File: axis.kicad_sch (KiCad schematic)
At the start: 46 parts, among them J101 CORTEX-DEBUG, J102 JAE_DX07S016JA3, SW101 SW_Push, SW102 SW_Push, U101 TPS78433QWDRBRQ1, U102 ATSAMD51G, U103 BMM150, U104 BHI160, Y101 32k768

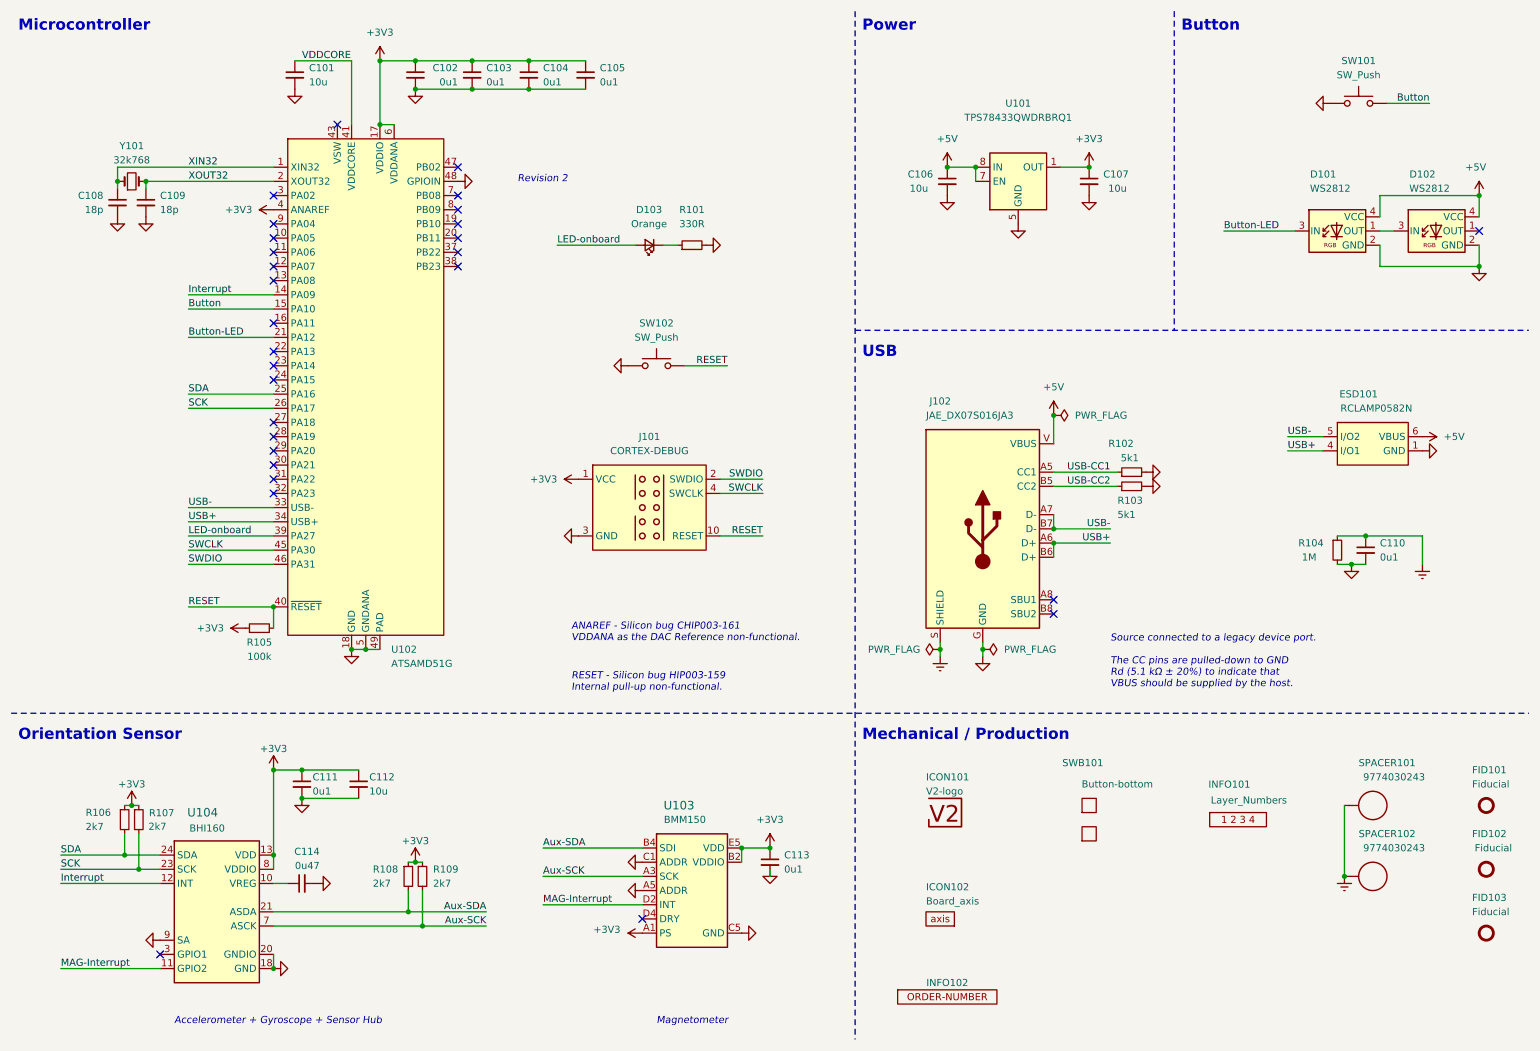
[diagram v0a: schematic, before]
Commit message: Replace standoffs
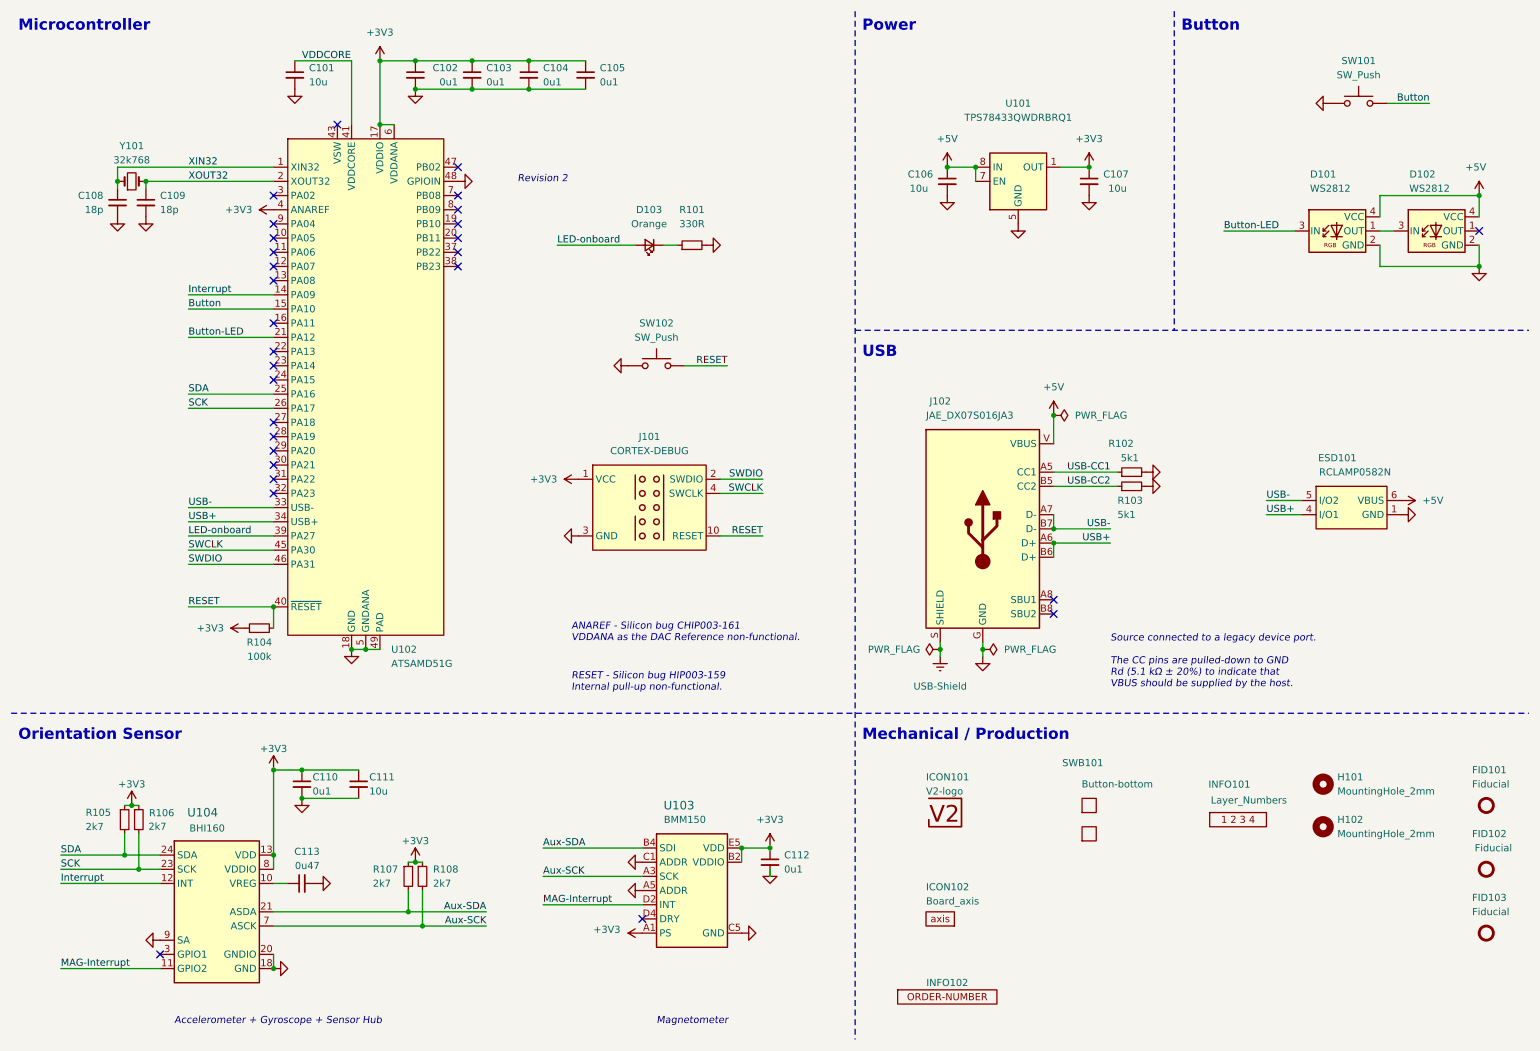
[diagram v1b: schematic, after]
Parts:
- removed C110: 0u1, Capacitor_SMD:C_0603_1608Metric, symbol Device:C_Small
- removed R104: 1M, Resistor_SMD:R_0603_1608Metric, symbol Device:R_Small
- removed SPACER101, SPACER102: 9774030243, V2_Spacer_Wurth:9774030243, symbol V2_Spacer_Wurth:9774030243
- added H101, H102: MountingHole_2mm, V2_Mechanical:MountingHole_2mm, symbol V2_Mechanical:MountingHole_2mm
- renumbered C111 to C110, C112 to C111, C113 to C112, C114 to C113, R105 to R104, R106 to R105, R107 to R106, R108 to R107, R109 to R108
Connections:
- net Earth renamed USB-Shield
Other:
- moved on the sheet: ESD101

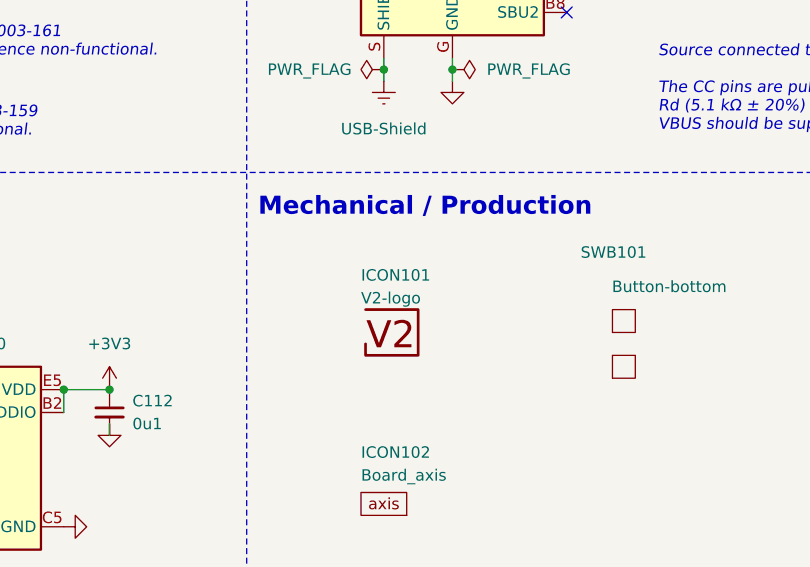
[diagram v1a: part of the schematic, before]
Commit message: Change capacitors
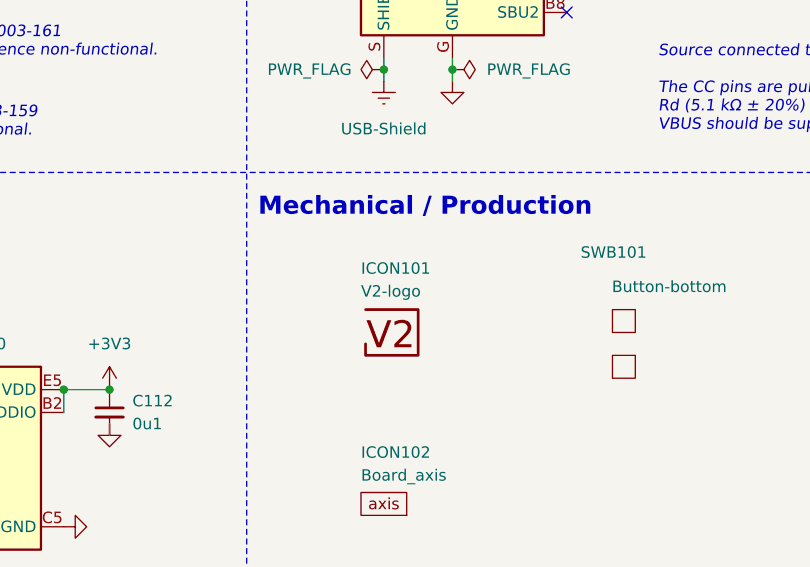
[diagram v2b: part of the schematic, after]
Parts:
- C106, C107: footprint Capacitor_SMD:C_0603_1608Metric -> Capacitor_SMD:C_0805_2012Metric
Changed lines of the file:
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@@
 	(title_block
 		(title "V2 axis")
-		(date "2025-10-26")
-		(rev "5")
+		(date "2025-11-16")
+		(rev "6")
 		(company "Versio Duo")
 		(comment 1 "Orientation Sensor")
@@
 			)
 		)
-		(property "Footprint" "Capacitor_SMD:C_0603_1608Metric"
+		(property "Footprint" "Capacitor_SMD:C_0805_2012Metric"
 			(at 205.74 43.18 0)
 			(effects
@@
 		(at 247.65 151.13 0)
 		(unit 1)
-		(exclude_from_sim no)
+		(exclude_from_sim yes)
 		(in_bom no)
 		(on_board yes)
@@
 			)
 		)
-		(property "Sim.Enable" "0"
-			(at 247.65 151.13 0)
-			(effects
-				(font
-					(size 1.27 1.27)
-				)
-				(hide yes)
-			)
-		)
 		(instances
 			(project ""
@@
 			)
 		)
-		(property "Footprint" "Capacitor_SMD:C_0603_1608Metric"
+		(property "Footprint" "Capacitor_SMD:C_0805_2012Metric"
 			(at 180.34 43.18 0)
 			(effects
@@
 		(dnp no)
 		(property "Reference" "ICON101"
-			(at 176.53 149.86 0)
+			(at 176.53 149.098 0)
 			(effects
 				(font
@@
 		)
 		(property "Value" "V2-logo"
-			(at 176.53 152.4 0)
+			(at 176.53 151.638 0)
 			(effects
 				(font

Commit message: Update
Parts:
- removed C110: 0u1, Capacitor_SMD:C_0603_1608Metric, symbol Device:C_Small
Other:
- moved on the sheet: C111
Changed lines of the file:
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@@
 	)
 	(junction
-		(at 64.77 148.59)
-		(diameter 0)
-		(color 0 0 0 0)
-	)
-	(junction
 		(at 105.41 26.67)
 		(diameter 0)
@@
 	)
 	(junction
-		(at 64.77 153.67)
-		(diameter 0)
-		(color 0 0 0 0)
-	)
-	(junction
 		(at 85.09 165.1)
 		(diameter 0)
@@
 	(wire
 		(pts
-			(xy 59.69 148.59) (xy 64.77 148.59)
-		)
-		(stroke
-			(width 0)
-			(type default)
-		)
-	)
-	(wire
-		(pts
 			(xy 148.59 167.64) (xy 148.59 166.37)
 		)
@@
 	(wire
 		(pts
-			(xy 64.77 153.67) (xy 74.93 153.67)
-		)
-		(stroke
-			(width 0)
-			(type default)
-		)
-	)
-	(wire
-		(pts
 			(xy 83.82 170.18) (xy 83.82 173.99)
 		)
@@
 	(wire
 		(pts
-			(xy 64.77 148.59) (xy 74.93 148.59)
+			(xy 59.69 148.59) (xy 64.77 148.59)
 		)
 		(stroke
@@
 	)
 	(symbol
-		(lib_id "Device:C_Small")
-		(at 64.77 151.13 0)
-		(unit 1)
-		(exclude_from_sim no)
-		(in_bom yes)
-		(on_board yes)
-		(dnp no)
-		(property "Reference" "C110"
-			(at 66.675 149.86 0)
-			(effects
-				(font
-					(size 1.27 1.27)
-				)
-				(justify left)
-			)
-		)
-		(property "Value" "0u1"
-			(at 66.675 152.4 0)
-			(effects
-				(font
-					(size 1.27 1.27)
-				)
-				(justify left)
-			)
-		)
-		(property "Footprint" "Capacitor_SMD:C_0603_1608Metric"
-			(at 64.77 151.13 0)
-			(effects
-				(font
-					(size 1.27 1.27)
-				)
-				(hide yes)
-			)
-		)
-		(property "Datasheet" "~"
-			(at 64.77 151.13 0)
-			(effects
-				(font
-					(size 1.27 1.27)
-				)
-				(hide yes)
-			)
-		)
-		(property "Description" ""
-			(at 64.77 151.13 0)
-			(effects
-				(font
-					(size 1.27 1.27)
-				)
-				(hide yes)
-			)
-		)
-		(pin "1"
-		)
-		(pin "2"
-		)
-		(instances
-			(project "axis"
-				(path "/6c8448b4-b04d-47e1-934e-e40cbe27a7be"
-					(reference "C110")
-					(unit 1)
-				)
-			)
-		)
-	)
-	(symbol
 		(lib_id "power:+3V3")
 		(at 54.61 123.19 90)
@@
 	(symbol
 		(lib_id "Device:C_Small")
-		(at 74.93 151.13 0)
+		(at 64.77 151.13 0)
 		(unit 1)
 		(exclude_from_sim no)
@@
 		(dnp no)
 		(property "Reference" "C111"
-			(at 76.835 149.86 0)
+			(at 66.675 149.86 0)
 			(effects
 				(font
@@
 		)
 		(property "Value" "10u"
-			(at 76.835 152.4 0)
+			(at 66.675 152.4 0)
 			(effects
 				(font
@@
 		)
 		(property "Footprint" "Capacitor_SMD:C_0603_1608Metric"
-			(at 74.93 151.13 0)
+			(at 64.77 151.13 0)
 			(effects
 				(font
@@
 		)
 		(property "Datasheet" "~"
-			(at 74.93 151.13 0)
+			(at 64.77 151.13 0)
 			(effects
 				(font
@@
 		)
 		(property "Description" ""
-			(at 74.93 151.13 0)
+			(at 64.77 151.13 0)
 			(effects
 				(font

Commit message: Colours
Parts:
- renumbered C111 to C110, C112 to C111, C113 to C112
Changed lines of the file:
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@@
 		(on_board yes)
 		(dnp no)
-		(property "Reference" "C112"
+		(property "Reference" "C111"
 			(at 151.13 163.83 0)
 			(effects
@@
 			(project "axis"
 				(path "/6c8448b4-b04d-47e1-934e-e40cbe27a7be"
-					(reference "C112")
+					(reference "C111")
 					(unit 1)
 				)
@@
 		(on_board yes)
 		(dnp no)
-		(property "Reference" "C113"
+		(property "Reference" "C112"
 			(at 67.945 163.195 90)
 			(effects
@@
 			(project "axis"
 				(path "/6c8448b4-b04d-47e1-934e-e40cbe27a7be"
-					(reference "C113")
+					(reference "C112")
 					(unit 1)
 				)
@@
 		(on_board yes)
 		(dnp no)
-		(property "Reference" "C111"
+		(property "Reference" "C110"
 			(at 66.675 149.86 0)
 			(effects
@@
 			(project "axis"
 				(path "/6c8448b4-b04d-47e1-934e-e40cbe27a7be"
-					(reference "C111")
+					(reference "C110")
 					(unit 1)
 				)
